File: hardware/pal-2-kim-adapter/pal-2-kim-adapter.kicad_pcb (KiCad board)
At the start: 2 copper layers, 21.7 x 112.9 mm, 4 parts, among them J1 Peripheral, J2 KIM-1, J3 RESET

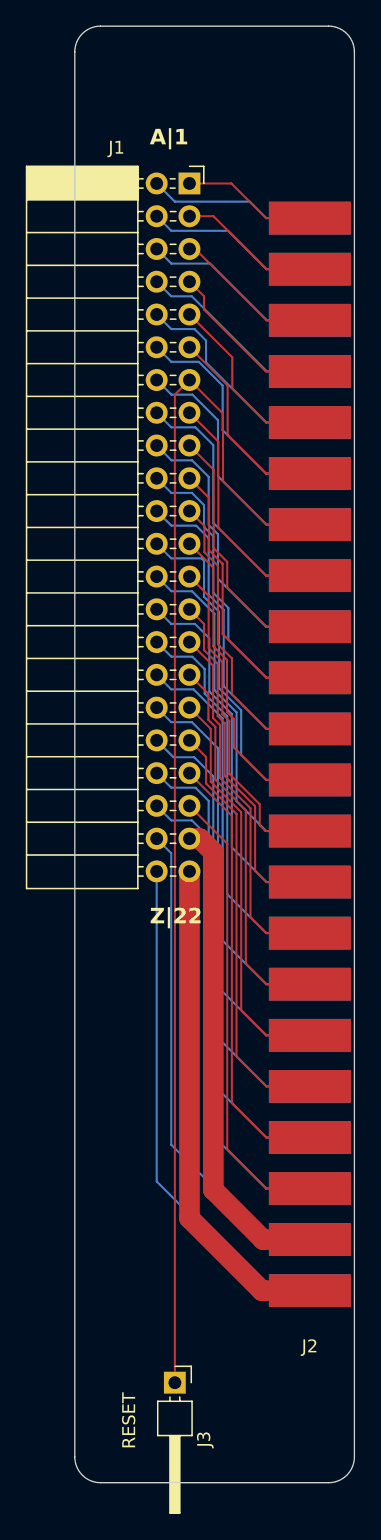
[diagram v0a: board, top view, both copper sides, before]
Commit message: Add forced DECEN for higher addresses to the PAL-2-KIM adapter
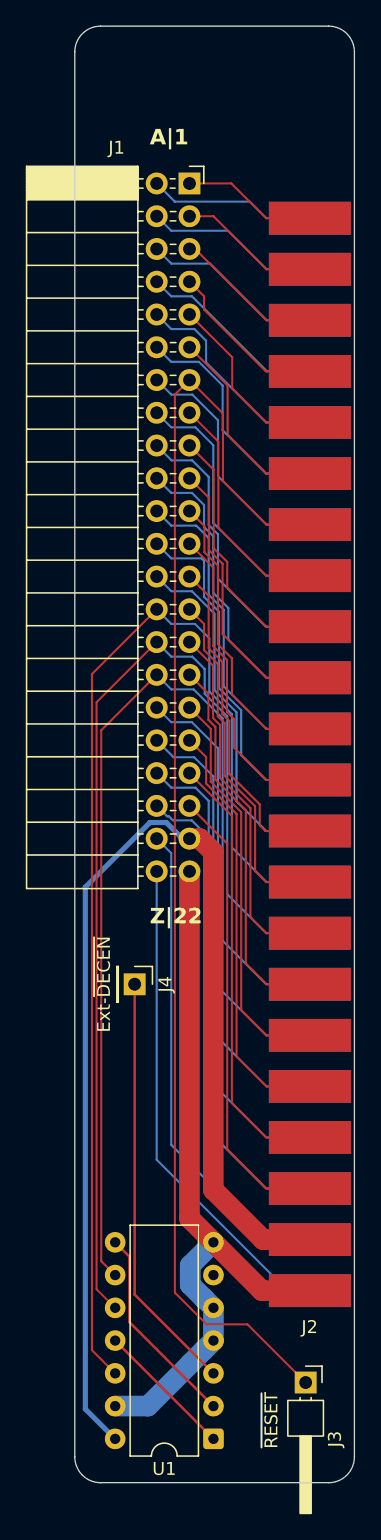
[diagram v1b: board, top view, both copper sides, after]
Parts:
- added J4: Ext-~{DECEN}, Connector_PinHeader_2.54mm:PinHeader_1x01_P2.54mm_Vertical, F.Cu at (147.4, 116.5)
- added U1: 74LS32, Package_DIP:DIP-14_W7.62mm, F.Cu at (153.5, 151.8)
- J3: value RESET -> ~{RESET}
- moved J3 10.1 mm to (160.7, 147.4)
- moved REF** 3.64 mm to (152.4, 123.2)
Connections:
- net Net-(J1-+5V) renamed +5V
- net Net-(J1-GND) renamed GND
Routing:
- net Net-(J1-A13): track 29.1 -> 91.2 mm
- net +5V: track 37.6 -> 92.0 mm
- net Net-(J1-A14): track 30.4 -> 84.6 mm
- net Net-(J1-A15): track 31.9 -> 80.7 mm
- net Net-(J4-Pin_1): track 0.00 -> 32.7 mm
- net GND: track 38.6 -> 57.4 mm
- net Net-(U1-Pad2): track 0.00 -> 15.9 mm
- net Net-(U1-Pad1): track 0.00 -> 10.8 mm
- net Net-(J1-~{RES}): track 95.3 -> 101.3 mm
- net Net-(J1-RAMRW): track 39.4 -> 38.4 mm
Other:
- board text removed: "RESET"
